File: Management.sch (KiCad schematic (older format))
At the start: 10 parts, among them J3 PDI, Q1 MMUN2231L, U1 ATXMEGA128A1U-AU, X1 16MHz, X2 32768

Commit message: Reannotate
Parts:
- renumbered C30 to C10, C31 to C11, C18 to C8, C19 to C9, J3 to J6, R12 to R9
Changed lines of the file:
@@
 P 5300 2700
 AR Path="/56F02951" Ref="J?"  Part="1"
-AR Path="/56F01E80/56F02951" Ref="J3"  Part="1"
-F 0 "J3" H 5300 2940 50  0000 C CNN
+AR Path="/56F01E80/56F02951" Ref="J6"  Part="1"
+F 0 "J6" H 5300 2940 50  0000 C CNN
 F 1 "PDI" H 5300 2849 50  0000 C CNN
 F 2 "conn-100mil:CONN-100MIL-M-2x3-SHROUD" H 5275 2700 50  0001 C CNN
@@
 P 6500 2800
 AR Path="/56F02971" Ref="C?"  Part="1"
-AR Path="/56F01E80/56F02971" Ref="C19"  Part="1"
-F 0 "C19" H 6613 2846 50  0000 L CNN
+AR Path="/56F01E80/56F02971" Ref="C9"  Part="1"
+F 0 "C9" H 6613 2846 50  0000 L CNN
 F 1 "15p" H 6613 2755 50  0000 L CNN
 F 2 "IPC7351-Nominal:CAPC1005X55" H 6500 2800 50  0001 C CNN
@@
 P 6100 2800
 AR Path="/56F02979" Ref="C?"  Part="1"
-AR Path="/56F01E80/56F02979" Ref="C18"  Part="1"
-F 0 "C18" H 6213 2846 50  0000 L CNN
+AR Path="/56F01E80/56F02979" Ref="C8"  Part="1"
+F 0 "C8" H 6213 2846 50  0000 L CNN
 F 1 "15p" H 6213 2755 50  0000 L CNN
 F 2 "IPC7351-Nominal:CAPC1005X55" H 6100 2800 50  0001 C CNN
@@
 P 6850 2600
 AR Path="/56F029AB" Ref="C?"  Part="1"
-AR Path="/56F01E80/56F029AB" Ref="C30"  Part="1"
-F 0 "C30" H 6737 2646 50  0000 R CNN
+AR Path="/56F01E80/56F029AB" Ref="C10"  Part="1"
+F 0 "C10" H 6737 2646 50  0000 R CNN
 F 1 "15p" H 6737 2555 50  0000 R CNN
 F 2 "IPC7351-Nominal:CAPC1005X55" H 6850 2600 50  0001 C CNN
@@
 P 7250 2600
 AR Path="/56F029B9" Ref="C?"  Part="1"
-AR Path="/56F01E80/56F029B9" Ref="C31"  Part="1"
-F 0 "C31" H 7363 2646 50  0000 L CNN
+AR Path="/56F01E80/56F029B9" Ref="C11"  Part="1"
+F 0 "C11" H 7363 2646 50  0000 L CNN
 F 1 "15p" H 7363 2555 50  0000 L CNN
 F 2 "IPC7351-Nominal:CAPC1005X55" H 7250 2600 50  0001 C CNN
@@
 P 4450 2950
 AR Path="/56F029E2" Ref="R?"  Part="3"
-AR Path="/56F01E80/56F029E2" Ref="R12"  Part="3"
-F 0 "R12" H 4387 2904 50  0000 R CNN
+AR Path="/56F01E80/56F029E2" Ref="R9"  Part="3"
+F 0 "R9" H 4387 2904 50  0000 R CNN
 F 1 "3k3" H 4387 2995 50  0000 R CNN
 F 2 "IPC7351-Nominal:RESCAXE80P160X320X70-8" H 4450 2950 50  0001 C CNN
@@
 P 4450 3200
 AR Path="/56F029EA" Ref="R?"  Part="4"
-AR Path="/56F01E80/56F029EA" Ref="R12"  Part="4"
-F 0 "R12" H 4513 3246 50  0000 L CNN
+AR Path="/56F01E80/56F029EA" Ref="R9"  Part="4"
+F 0 "R9" H 4513 3246 50  0000 L CNN
 F 1 "3k3" H 4513 3155 50  0000 L CNN
 F 2 "IPC7351-Nominal:RESCAXE80P160X320X70-8" H 4450 3200 50  0001 C CNN

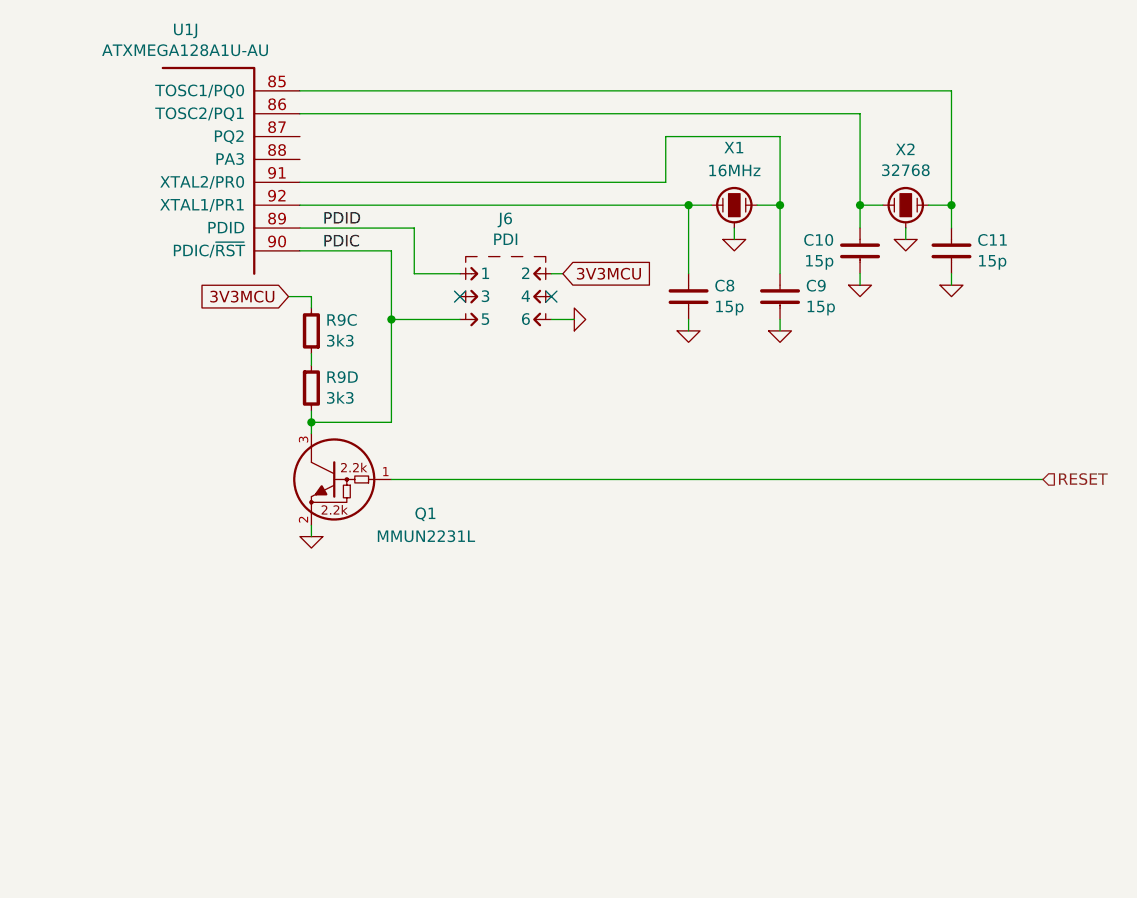
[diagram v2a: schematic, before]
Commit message: Schematic tidy-ups and add VBUS sense
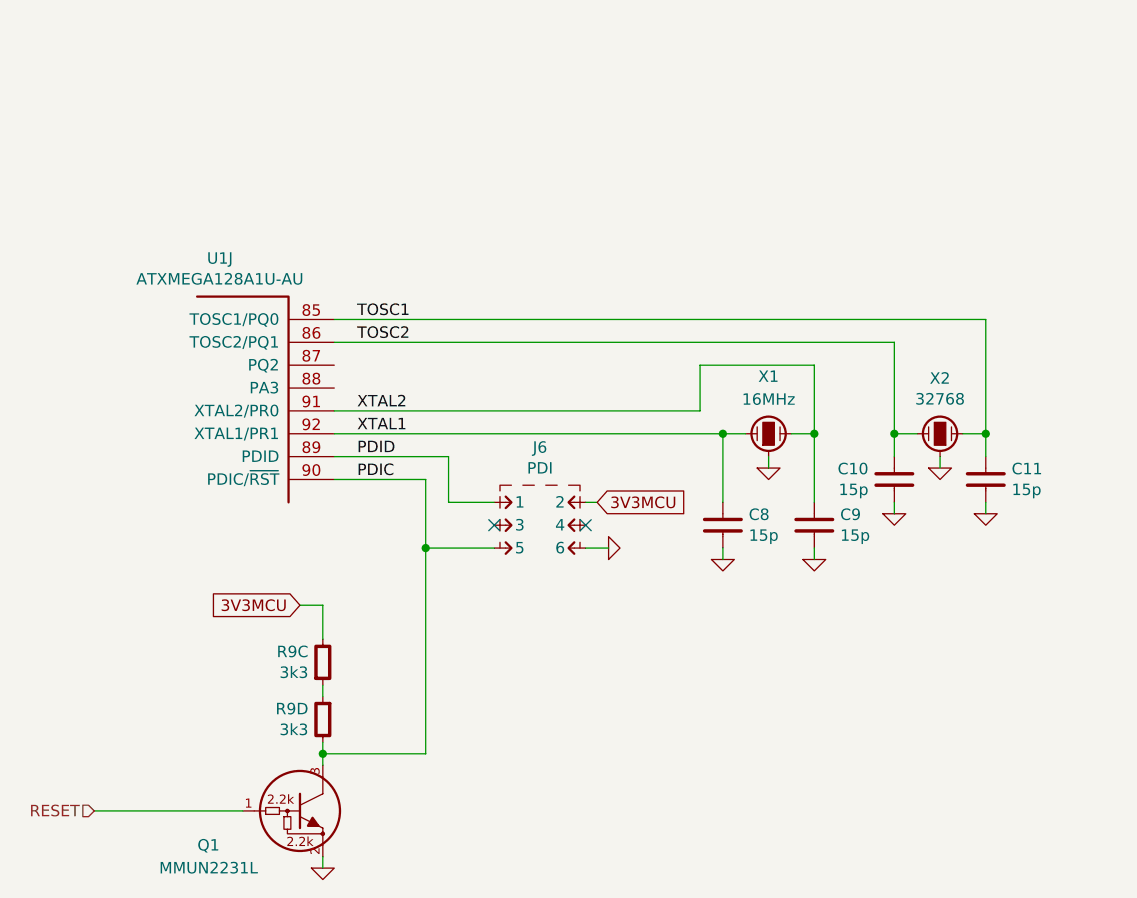
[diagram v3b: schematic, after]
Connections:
- net TOSC1: now reaches C11.1, U1.85 (TOSC1/PQ0), X2.1
- net TOSC2: now reaches C10.1, U1.86 (TOSC2/PQ1), X2.2
- net XTAL2: now reaches C9.1, U1.91 (XTAL2/PR0), X1.2
- net XTAL1: now reaches C8.1, U1.92 (XTAL1/PR1), X1.1
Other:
- moved on the sheet: C10, C11, C8, C9, J6, Q1, R9C, R9D, U1J, X1, X2

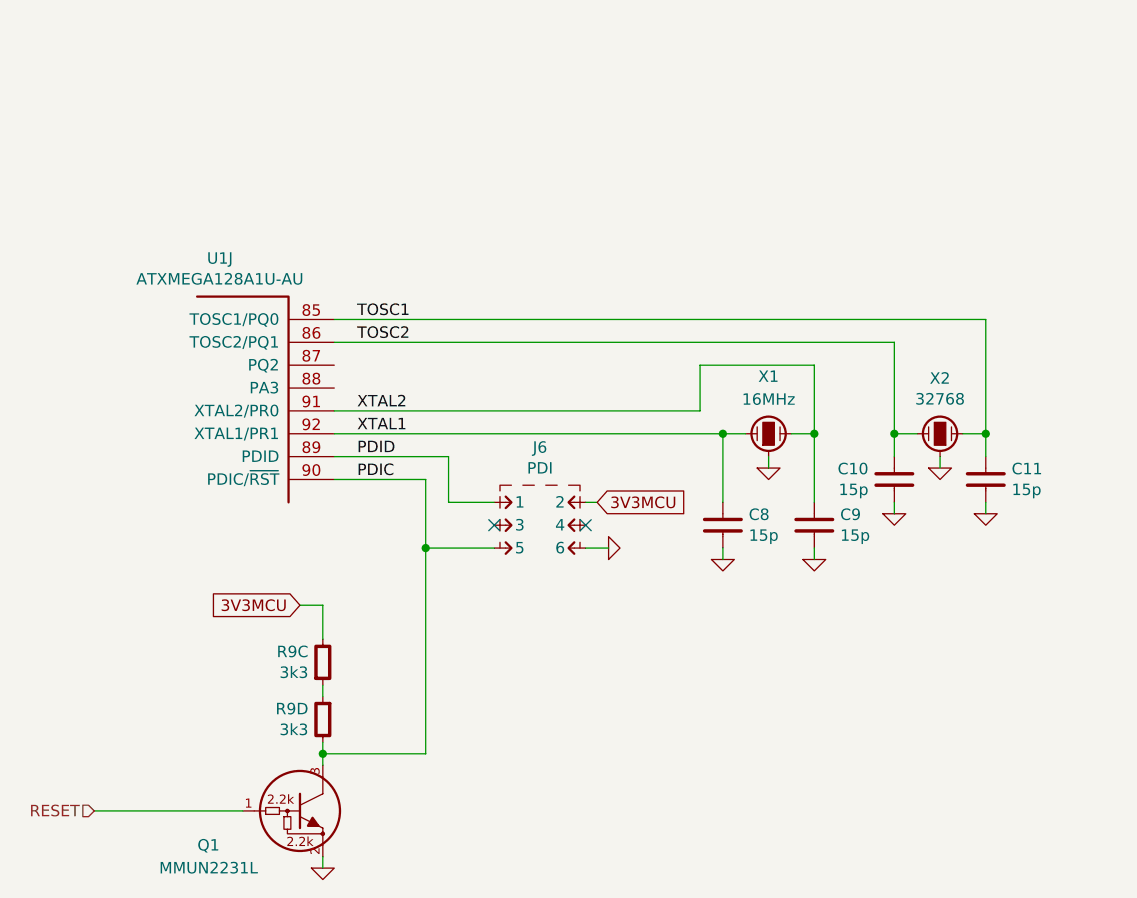
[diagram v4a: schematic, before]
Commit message: Bugfix: crystal capacitance too high
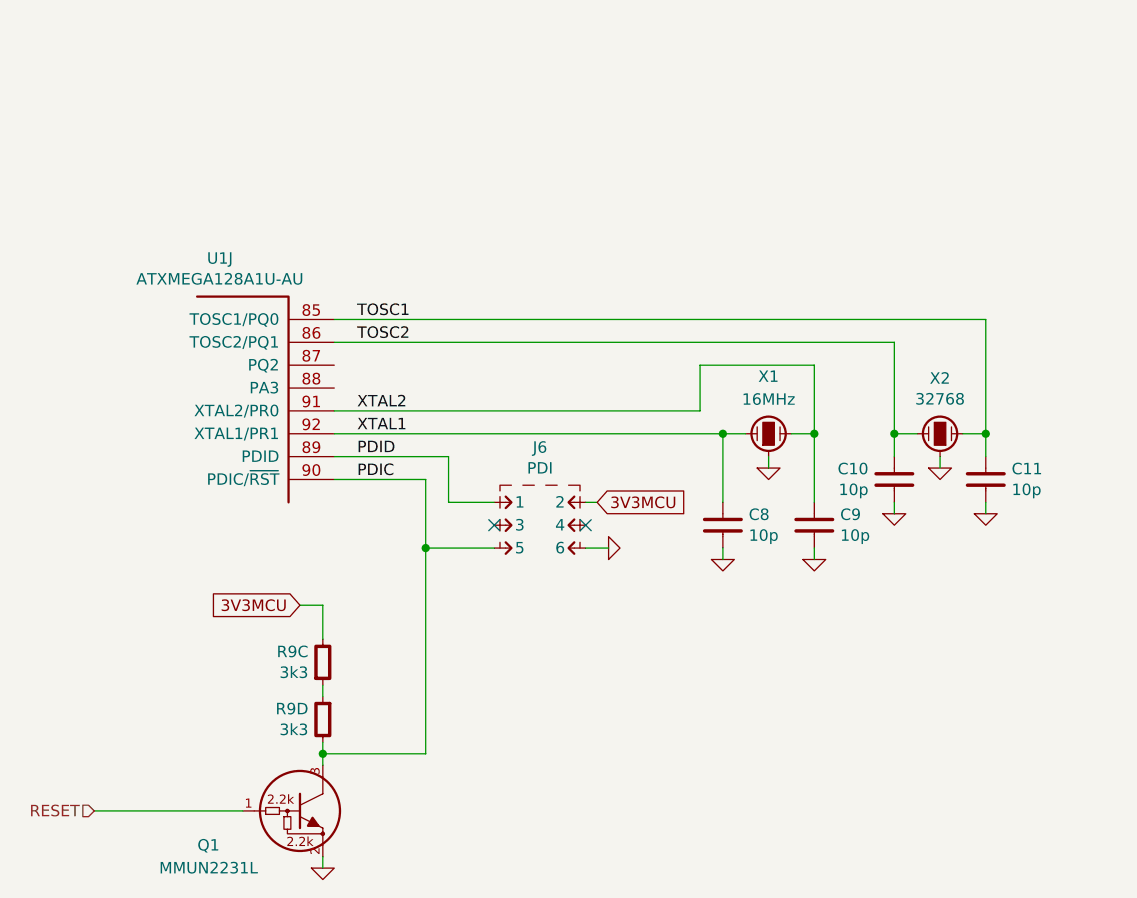
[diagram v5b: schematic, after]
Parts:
- C10, C11, C8, C9: value 15p -> 10p; BOM CAP MLCC 15p C0G 5% [0402] -> CAP MLCC 10p C0G 1% [0402]
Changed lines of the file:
@@
 AR Path="/56F01E80/56F02971" Ref="C9"  Part="1"
 F 0 "C9" H 6763 3846 50  0000 L CNN
-F 1 "15p" H 6763 3755 50  0000 L CNN
+F 1 "10p" H 6763 3755 50  0000 L CNN
 F 2 "IPC7351-Nominal:CAPC1005X55" H 6650 3800 50  0001 C CNN
 F 3 "" H 6640 3775 60  0000 C CNN
-F 4 "CAP MLCC 15p C0G 5% [0402]" H 7450 4350 60  0001 C CNN "BOM"
+F 4 "CAP MLCC 10p C0G 1% [0402]" H 7450 4350 60  0001 C CNN "BOM"
 	1    6650 3800
 	1    0    0    -1
@@
 AR Path="/56F01E80/56F02979" Ref="C8"  Part="1"
 F 0 "C8" H 6363 3846 50  0000 L CNN
-F 1 "15p" H 6363 3755 50  0000 L CNN
+F 1 "10p" H 6363 3755 50  0000 L CNN
 F 2 "IPC7351-Nominal:CAPC1005X55" H 6250 3800 50  0001 C CNN
 F 3 "" H 6240 3775 60  0000 C CNN
-F 4 "CAP MLCC 15p C0G 5% [0402]" H 7050 4350 60  0001 C CNN "BOM"
+F 4 "CAP MLCC 10p C0G 1% [0402]" H 7050 4350 60  0001 C CNN "BOM"
 	1    6250 3800
 	1    0    0    -1
@@
 AR Path="/56F01E80/56F029AB" Ref="C10"  Part="1"
 F 0 "C10" H 6887 3646 50  0000 R CNN
-F 1 "15p" H 6887 3555 50  0000 R CNN
+F 1 "10p" H 6887 3555 50  0000 R CNN
 F 2 "IPC7351-Nominal:CAPC1005X55" H 7000 3600 50  0001 C CNN
 F 3 "" H 6990 3575 60  0000 C CNN
-F 4 "CAP MLCC 15p C0G 5% [0402]" H 7800 4150 60  0001 C CNN "BOM"
+F 4 "CAP MLCC 10p C0G 1% [0402]" H 7800 4150 60  0001 C CNN "BOM"
 	1    7000 3600
 	1    0    0    -1
@@
 AR Path="/56F01E80/56F029B9" Ref="C11"  Part="1"
 F 0 "C11" H 7513 3646 50  0000 L CNN
-F 1 "15p" H 7513 3555 50  0000 L CNN
+F 1 "10p" H 7513 3555 50  0000 L CNN
 F 2 "IPC7351-Nominal:CAPC1005X55" H 7400 3600 50  0001 C CNN
 F 3 "" H 7390 3575 60  0000 C CNN
-F 4 "CAP MLCC 15p C0G 5% [0402]" H 8200 4150 60  0001 C CNN "BOM"
+F 4 "CAP MLCC 10p C0G 1% [0402]" H 8200 4150 60  0001 C CNN "BOM"
 	1    7400 3600
 	1    0    0    -1
@@
 	5750 3900 5650 3900
 Wire Wire Line
-	4950 3600 4950 3900
-Wire Wire Line
-	4950 3900 4950 4800
-Wire Wire Line
-	4550 3400 6250 3400
-Wire Wire Line
-	6250 3400 6350 3400
+	4950 3600 4950 4800
+Wire Wire Line
+	4550 3400 6350 3400
 Wire Wire Line
 	4550 3300 6150 3300
 Wire Wire Line
-	6650 3100 6650 3400
-Wire Wire Line
-	6650 3400 6650 3700
+	6650 3100 6650 3700
 Wire Wire Line
 	6650 3400 6550 3400
@@
 	6650 3950 6650 3900
 Wire Wire Line
-	4500 4750 4500 4800
-Wire Wire Line
-	4500 4800 4500 4850
+	4500 4750 4500 4850
 Wire Wire Line
 	4500 5300 4500 5250
@@
 	7100 3400 7000 3400
 Wire Wire Line
-	7000 3000 7000 3400
-Wire Wire Line
-	7000 3400 7000 3500
+	7000 3000 7000 3500
 Wire Wire Line
 	7000 3750 7000 3700
@@
 	7300 3400 7400 3400
 Wire Wire Line
-	7400 2900 7400 3400
-Wire Wire Line
-	7400 3400 7400 3500
+	7400 2900 7400 3500
 Wire Wire Line
 	7400 3750 7400 3700

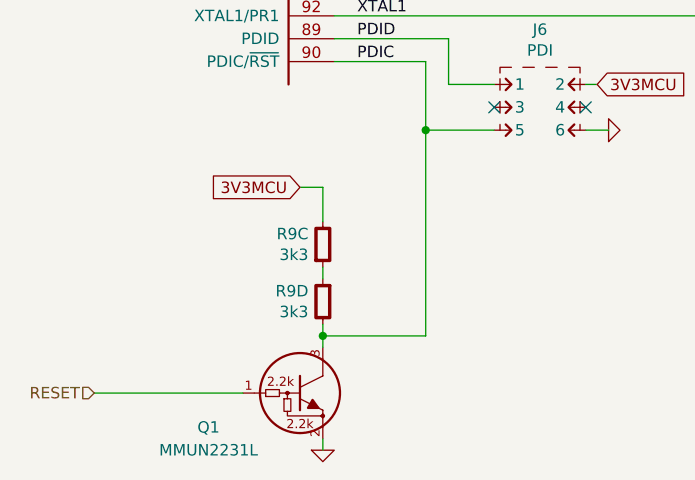
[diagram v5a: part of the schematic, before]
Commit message: Decrease LED current
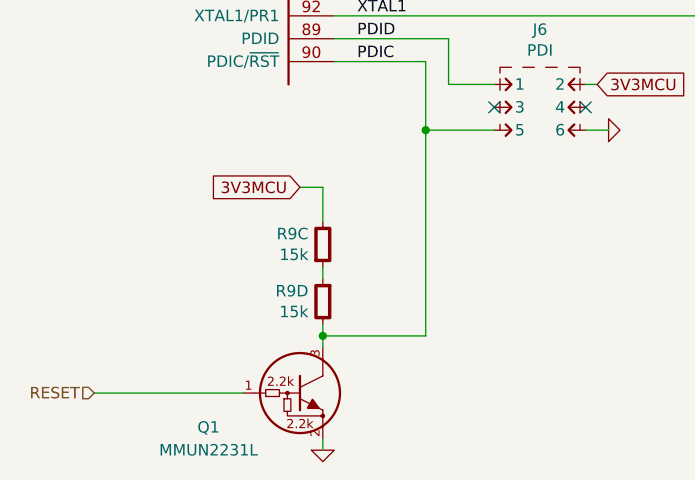
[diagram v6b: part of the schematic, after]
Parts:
- R9: value 3k3 -> 15k; BOM DIST DIGIKEY YC164J-3.3KCT-ND -> DIST DIGIKEY YC164J-15KCT-ND
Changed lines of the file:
@@
 AR Path="/56F01E80/56F029E2" Ref="R9"  Part="3"
 F 0 "R9" H 4437 4354 50  0000 R CNN
-F 1 "3k3" H 4437 4445 50  0000 R CNN
+F 1 "15k" H 4437 4445 50  0000 R CNN
 F 2 "IPC7351-Nominal:RESCAXE80P160X320X70-8" H 4500 4400 50  0001 C CNN
 F 3 "" H 4500 4450 60  0000 C CNN
-F 4 "DIST DIGIKEY YC164J-3.3KCT-ND" H 4500 4400 60  0001 C CNN "BOM"
+F 4 "DIST DIGIKEY YC164J-15KCT-ND" H 4500 4400 60  0001 C CNN "BOM"
 	3    4500 4400
 	1    0    0    1
@@
 AR Path="/56F01E80/56F029EA" Ref="R9"  Part="4"
 F 0 "R9" H 4563 4696 50  0000 L CNN
-F 1 "3k3" H 4563 4605 50  0000 L CNN
+F 1 "15k" H 4563 4605 50  0000 L CNN
 F 2 "IPC7351-Nominal:RESCAXE80P160X320X70-8" H 4500 4650 50  0001 C CNN
 F 3 "" H 4500 4700 60  0000 C CNN
-F 4 "DIST DIGIKEY YC164J-3.3KCT-ND" H 4500 4650 60  0001 C CNN "BOM"
+F 4 "DIST DIGIKEY YC164J-15KCT-ND" H 4500 4650 60  0001 C CNN "BOM"
 	4    4500 4650
 	-1   0    0    -1

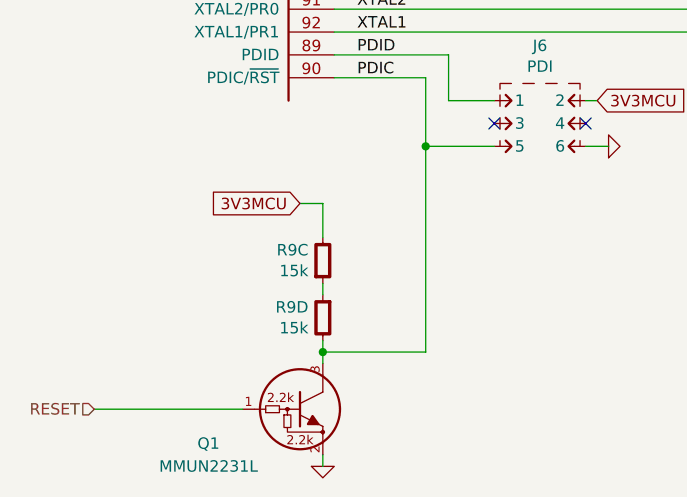
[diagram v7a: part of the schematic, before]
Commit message: Decrease reset pullup
Changing the LED resistors increased it
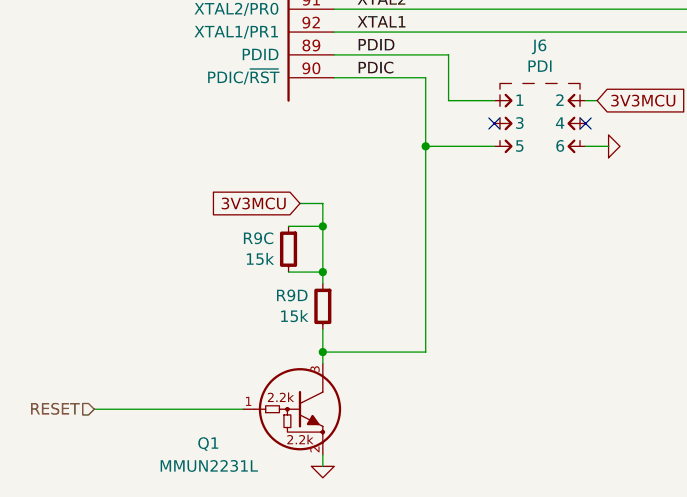
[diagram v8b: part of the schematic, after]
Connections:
- net 3V3MCU: now also R9.3, R9.4
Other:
- moved on the sheet: R9D
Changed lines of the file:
@@
 Sheet 4 5
 Title "XMEGA AU development board"
-Date "2016-03-22"
-Rev "A"
+Date "2016-04-01"
+Rev "B"
 Comp "SEMIANALOG"
 Comment1 "DEV-XMEGA-AU"
@@
 $Comp
 L RESPACK-4X0603-CONV R?
-U 3 1 56F029E2
-P 4500 4400
-AR Path="/56F029E2" Ref="R?"  Part="3"
-AR Path="/56F01E80/56F029E2" Ref="R9"  Part="3"
-F 0 "R9" H 4437 4354 50  0000 R CNN
-F 1 "15k" H 4437 4445 50  0000 R CNN
-F 2 "IPC7351-Nominal:RESCAXE80P160X320X70-8" H 4500 4400 50  0001 C CNN
-F 3 "" H 4500 4450 60  0000 C CNN
-F 4 "DIST DIGIKEY YC164J-15KCT-ND" H 4500 4400 60  0001 C CNN "BOM"
-	3    4500 4400
-	1    0    0    1
-$EndComp
-$Comp
-L RESPACK-4X0603-CONV R?
 U 4 1 56F029EA
-P 4500 4650
+P 4500 4600
 AR Path="/56F029EA" Ref="R?"  Part="4"
 AR Path="/56F01E80/56F029EA" Ref="R9"  Part="4"
-F 0 "R9" H 4563 4696 50  0000 L CNN
-F 1 "15k" H 4563 4605 50  0000 L CNN
-F 2 "IPC7351-Nominal:RESCAXE80P160X320X70-8" H 4500 4650 50  0001 C CNN
-F 3 "" H 4500 4700 60  0000 C CNN
-F 4 "DIST DIGIKEY YC164J-15KCT-ND" H 4500 4650 60  0001 C CNN "BOM"
-	4    4500 4650
+F 0 "R9" H 4563 4646 50  0000 L CNN
+F 1 "15k" H 4563 4555 50  0000 L CNN
+F 2 "IPC7351-Nominal:RESCAXE80P160X320X70-8" H 4500 4600 50  0001 C CNN
+F 3 "" H 4500 4650 60  0000 C CNN
+F 4 "DIST DIGIKEY YC164J-15KCT-ND" H 4500 4600 60  0001 C CNN "BOM"
+	4    4500 4600
 	-1   0    0    -1
 $EndComp
@@
 	6650 3950 6650 3900
 Wire Wire Line
-	4500 4750 4500 4850
+	4500 4700 4500 4850
 Wire Wire Line
 	4500 5300 4500 5250
 Wire Wire Line
-	4500 4500 4500 4550
+	4500 4150 4500 4500
 Wire Wire Line
 	7100 3400 7000 3400
@@
 Wire Wire Line
 	4400 4150 4500 4150
-Wire Wire Line
-	4500 4150 4500 4300
 Text GLabel 5700 3700 2    50   Input ~ 0
 3V3MCU
@@
 Text Label 4650 3300 0    50   ~ 0
 XTAL2
+$Comp
+L RESPACK-4X0603-CONV R?
+U 3 1 56FF0BB0
+P 4350 4350
+AR Path="/56FF0BB0" Ref="R?"  Part="4"
+AR Path="/56F01E80/56FF0BB0" Ref="R9"  Part="3"
+F 0 "R9" H 4413 4396 50  0000 L CNN
+F 1 "15k" H 4413 4305 50  0000 L CNN
+F 2 "IPC7351-Nominal:RESCAXE80P160X320X70-8" H 4350 4350 50  0001 C CNN
+F 3 "" H 4350 4400 60  0000 C CNN
+F 4 "DIST DIGIKEY YC164J-15KCT-ND" H 4350 4350 60  0001 C CNN "BOM"
+	3    4350 4350
+	-1   0    0    -1
+$EndComp
+Wire Wire Line
+	4350 4250 4500 4250
+Connection ~ 4500 4250
+Wire Wire Line
+	4350 4450 4500 4450
+Connection ~ 4500 4450
 $EndSCHEMATC
